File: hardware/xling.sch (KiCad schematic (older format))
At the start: 59 parts, among them J2 TPS63031, J3 MCP73831, J4 USB_OTG, J5 AVR ISP, J6 Battery, Q1 TP0610T, SW1 Reset, SW2 Up, SW3 Select, SW4 Down, U1 SH1106G, U2 ATMEGA128-16AU, Y1 8MHz

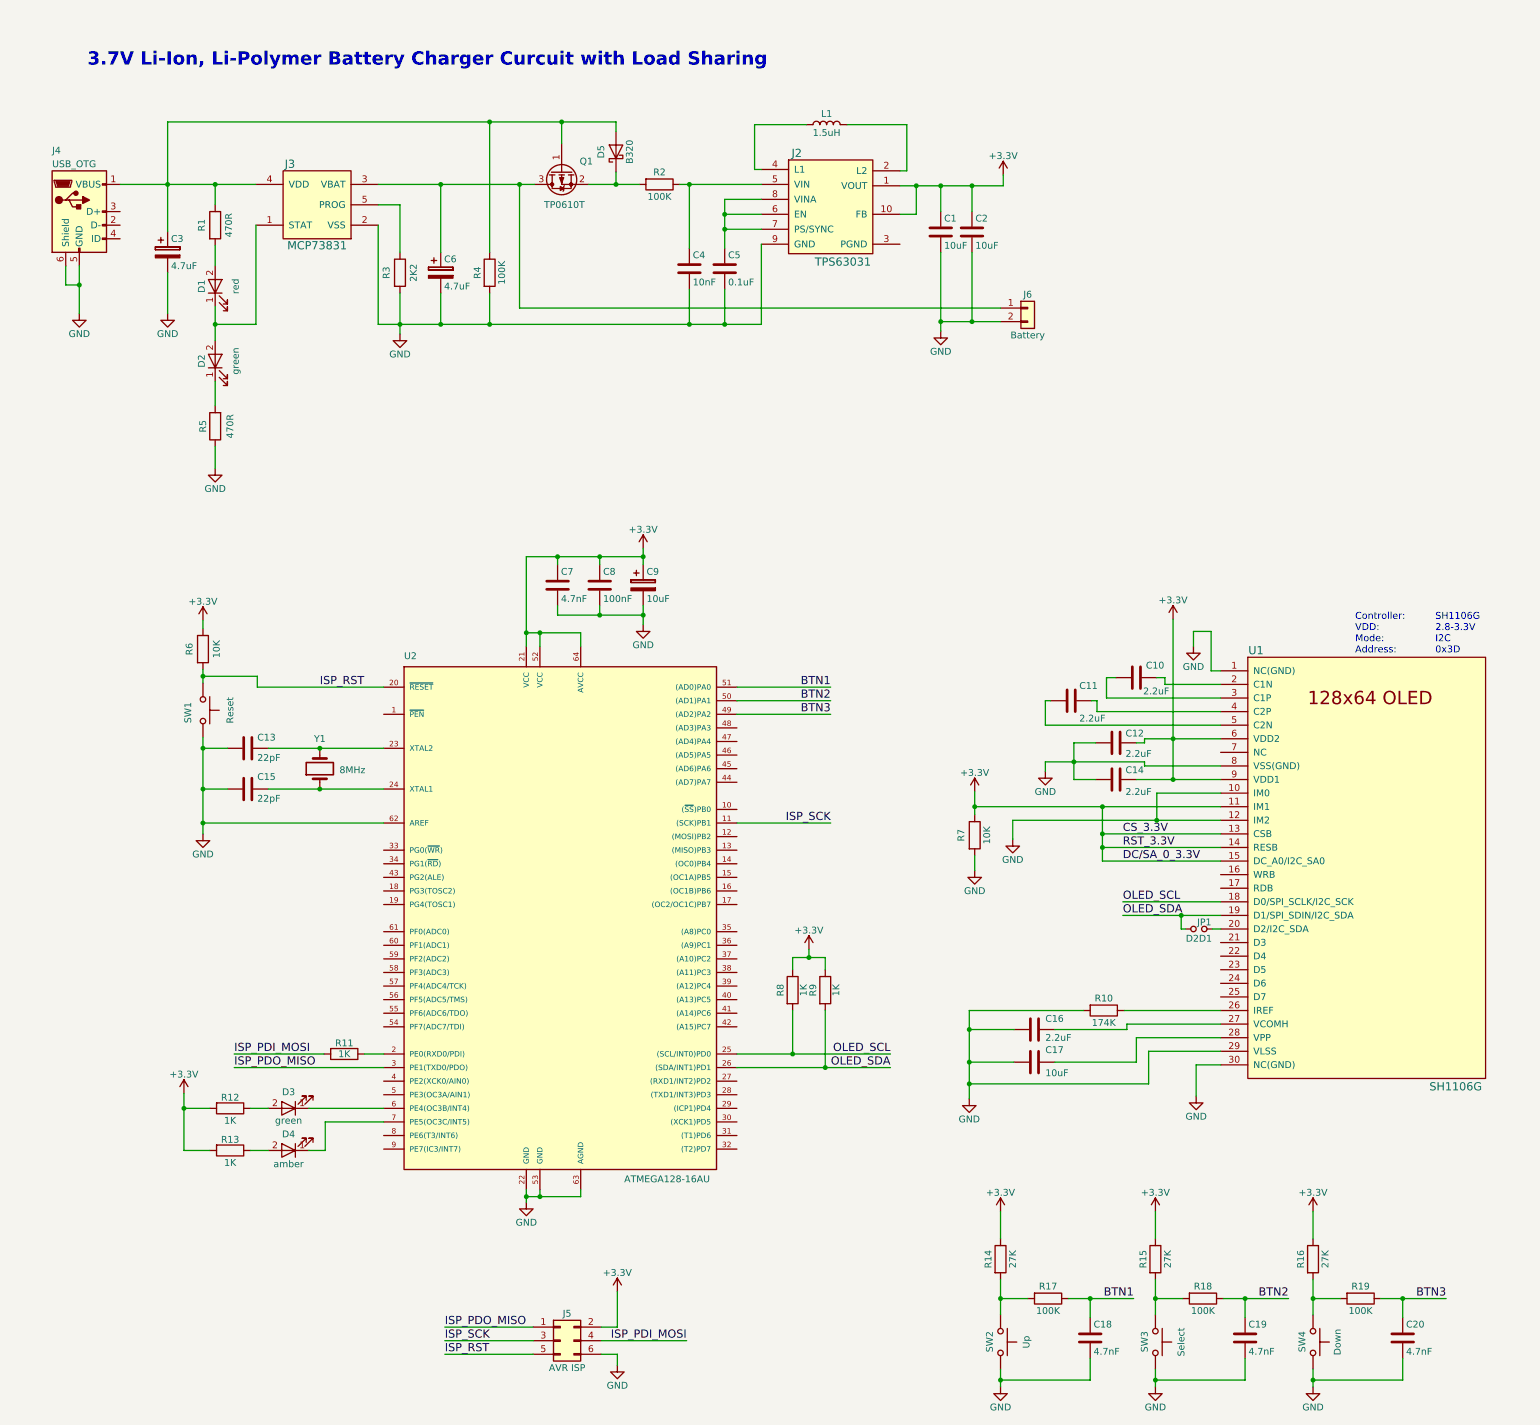
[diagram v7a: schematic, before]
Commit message: patch 0.1.8: Add other OLED and DCDC 3V-to-12V.
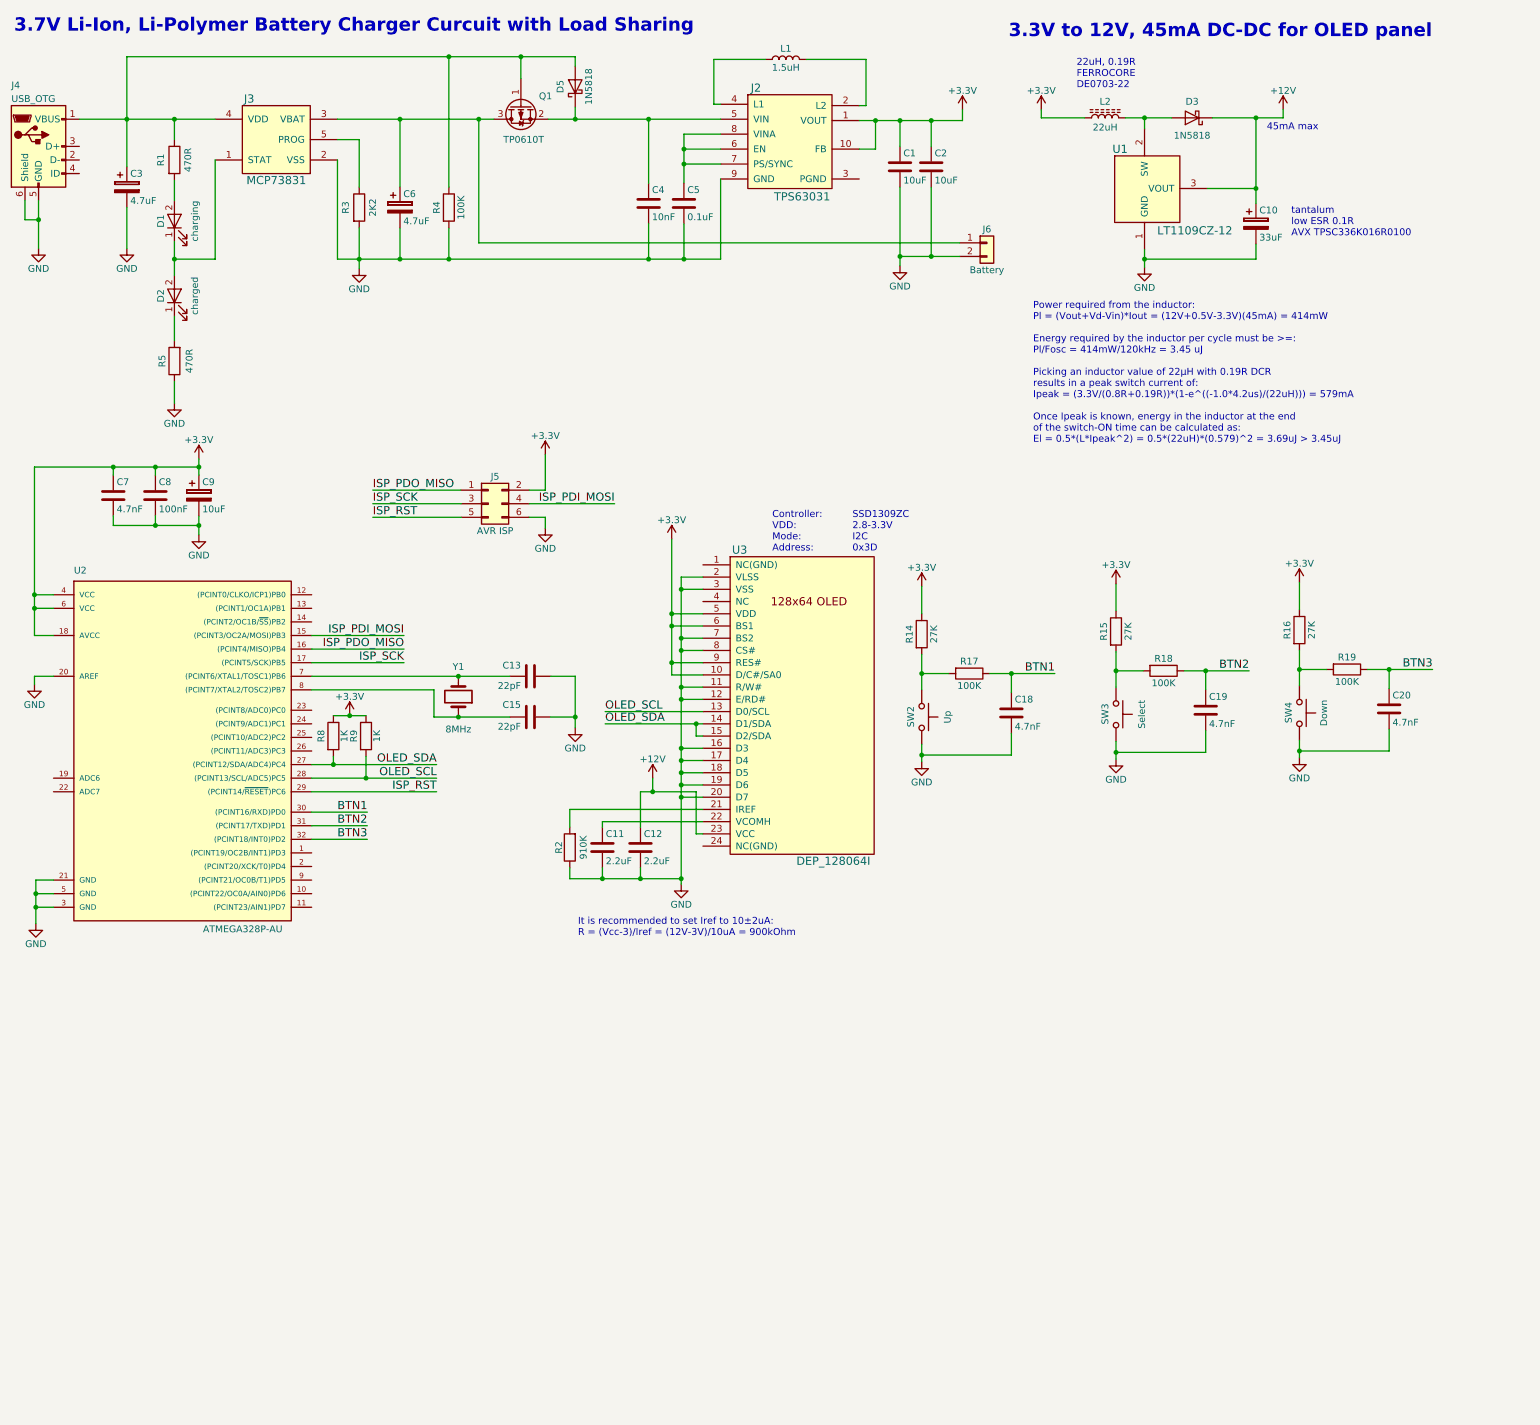
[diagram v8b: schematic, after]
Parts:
- removed C10, C14, C16: 2.2uF, Capacitors_SMD:C_0603, symbol C
- removed C17: 10uF, Capacitors_SMD:C_0805, symbol C
- removed D3: green, LEDs:LED_0805, symbol LED
- removed D4: amber, LEDs:LED_0603, symbol LED
- removed JP1: D2D1, Pin_Headers:Pin_Header_Straight_1x02, symbol Jumper_NO_Small
- removed R10: 174K, Resistors_SMD:R_0805, symbol R
- removed R11, R12, R13: 1K, Resistors_SMD:R_0603, symbol R
- removed R6, R7: 10K, Resistors_SMD:R_1206, symbol R
- removed SW1: Reset, Buttons_Switches_THT:SW_PUSH_6mm, symbol SW_Push
- removed U1: SH1106G, Xling Footprints:Connector_FFC_FPC_MOLEX_524353071_30-pins, symbol SH1106G
- removed U2: ATMEGA128-16AU, Xling Footprints:ATmega128_64-lead_14x14x1.0mm_TQFP, symbol ATMEGA128-16AU
- added C10: 33uF, symbol CP
- added D3: 1N5818, Diodes_THT:D_DO-41_SOD81_P7.62mm_Horizontal, symbol 1N5818
- added L2: 22uH, symbol L_Core_Ferrite
- added U1: LT1109CZ-12, symbol LT1109CZ-12
- added U2: ATMEGA328P-AU, Housings_QFP:TQFP-32_7x7mm_Pitch0.8mm, symbol ATMEGA328P-AU
- added U3: DEP_128064I, symbol DEP_128064I
- C11, C12: footprint Capacitors_SMD:C_0603 -> (none)
- C3, C6: footprint Capacitors_SMD:CP_Elec_10x10 -> Capacitors_SMD:CP_Elec_4x5.3
- D1: value red -> charging
- D2: value green -> charged
- D5: value B320 -> 1N5818; footprint Diodes_SMD:SMC_Standard -> Diodes_THT:D_DO-41_SOD81_P7.62mm_Horizontal
- R2: value 100K -> 910K; footprint Resistors_SMD:R_1206 -> (none)
- SW2, SW3, SW4: footprint Buttons_Switches_THT:SW_PUSH_6mm -> Buttons_Switches_SMD:SW_SPST_PTS645
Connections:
- net +3V3: now also L2.1, U2.18 (AVCC), U2.4 (VCC), U2.6 (VCC), U3.10 (D/C#/SA0), U3.5 (VDD), U3.6 (BS1), U3.9 (RES#); no longer C12.1
- net BTN1: now also U2.30 ((PCINT16/RXD)PD0)
- net BTN2: now also U2.31 ((PCINT17/TXD)PD1)
- net BTN3: now also U2.32 ((PCINT18/INT0)PD2)
- net GND: now also C11.2, R2.1, C10.2, U1.1 (GND), U2.20 (AREF), U2.21 (GND), U2.3 (GND), U2.5 (GND), U3.11 (R/W#), U3.12 (E/RD#), U3.16 (D3), U3.17 (D4), U3.18 (D5), U3.19 (D6), U3.2 (VLSS), U3.20 (D7), U3.3 (VSS), U3.7 (BS2), U3.8 (CS#)
- net ISP_PDI_MOSI: now also U2.15 ((PCINT3/OC2A/MOSI)PB3)
- net ISP_PDO_MISO: now also U2.16 ((PCINT4/MISO)PB4)
- net ISP_RST: now also U2.29 ((PCINT14/~RESET~)PC6)
- net ISP_SCK: now also U2.17 ((PCINT5/SCK)PB5)
- net OLED_SCL: now also R9.2, U2.28 ((PCINT13/SCL/ADC5)PC5), U3.13 (D0/SCL); no longer R8.2
- net OLED_SDA: now also R8.2, U2.27 ((PCINT12/SDA/ADC4)PC4), U3.14 (D1/SDA), U3.15 (D2/SDA); no longer R9.2
- net at C13.1, Y1.2: now also U2.7 ((PCINT6/XTAL1/TOSC1)PB6)
- net at C15.1, Y1.1: now also U2.8 ((PCINT7/XTAL2/TOSC2)PB7)
- net at C11.1: now also U3.22 (VCOMH)
- net at C4.1, J2.5 (VIN): now also D5.1 (K), Q1.2 (S); no longer R2.1
- new net: R2.2, U3.21 (IREF)
- new net: D3.2 (A), L2.2, U1.2 (SW)
- new net +12V: C10.1, C12.1, D3.1 (K), U1.3 (VOUT), U3.23 (VCC)
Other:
- note added: "22uH, 0.19R\nFERROCORE\nDE0703-22"
- note added: "3.3V to 12V, 45mA DC-DC for OLED panel"
- note added: "45mA max"
- note added: "It is recommended to set Iref to 10±2uA:\nR = (Vcc-3)/Iref = (12V-3V)/10uA = 900kOhm"
- note added: "Power required from the inductor:\nPl = (Vout+Vd-Vin)*Iout = (12V+0.5V-3.3V)(45mA) = 414mW\n\nEnergy required by the inductor per cycle must be >=:\nPl/Fosc = 414mW/120kHz = 3.45 uJ\n\nPicking an inductor value of 22μH with 0.19R DCR\nresults in a peak switch current of:\nIpeak = (3.3V/(0.8R+0.19R))*(1-e^((-1.0*4.2us)/(22uH))) = 579mA\n\nOnce Ipeak is known, energy in the inductor at the end\nof 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"
- note added: "SSD1309ZC\n2.8-3.3V\nI2C\n0x3D"
- note added: "tantalum\nlow ESR 0.1R\nAVX TPSC336K016R0100"
- note removed: "SH1106G\n2.8-3.3V\nI2C\n0x3D"
- moved on the sheet: C1, C13, C15, C18, C19, C2, C20, C3, C4, C5, C6, C7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
